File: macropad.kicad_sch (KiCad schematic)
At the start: 1 part, among them U1 RP2040

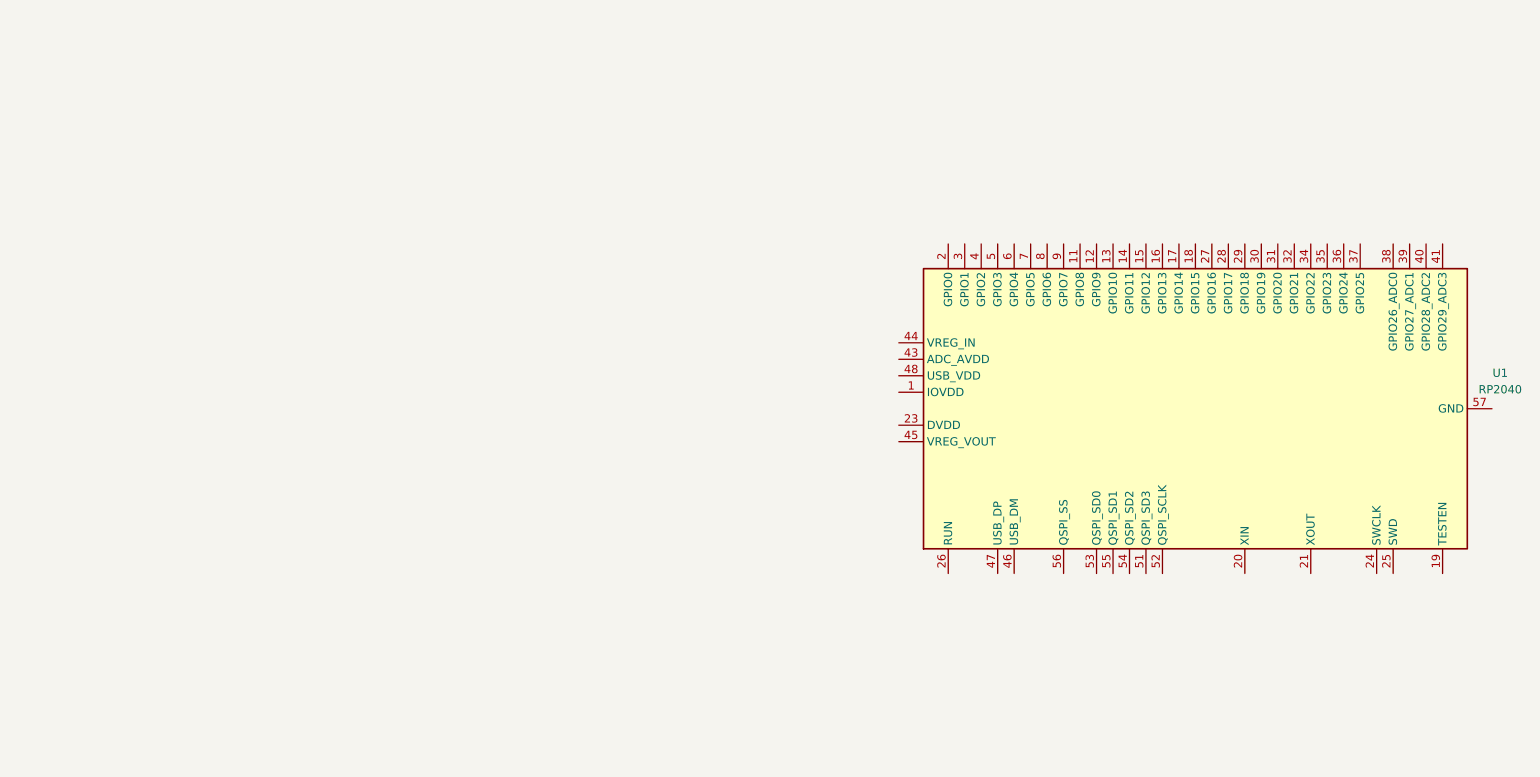
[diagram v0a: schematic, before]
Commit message: Make switches and rotary encoder
Got a rotary encoder switch and hooked it up to the MCU
Imported Joe Scotto's symbols and footprints for switches
Assigned footprint for diodes
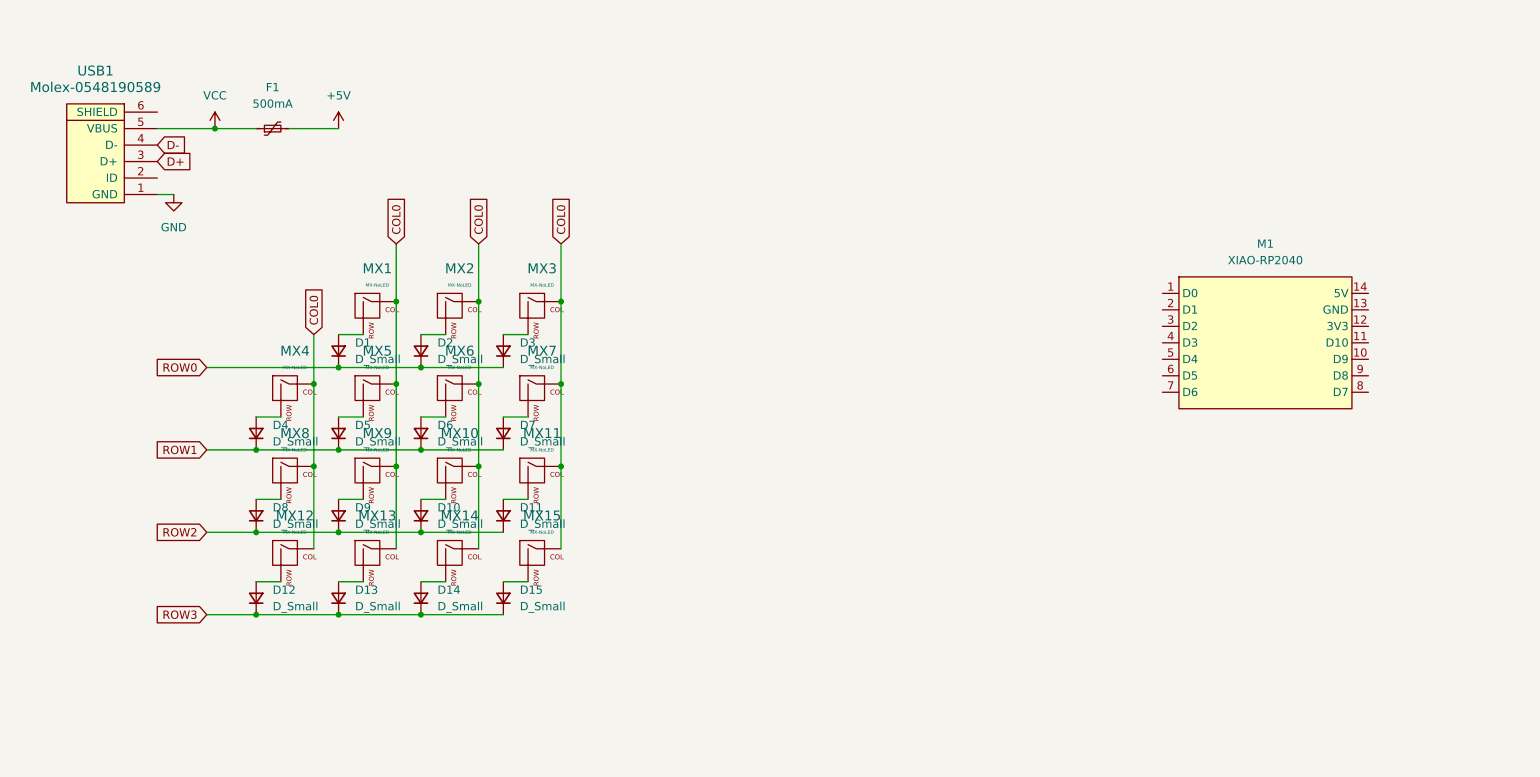
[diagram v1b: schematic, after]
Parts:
- removed U1: RP2040, Package_DFN_QFN:QFN-56-1EP_7x7mm_P0.4mm_EP3.2x3.2mm, symbol MCU_RaspberryPi:RP2040
- added D1, D10, D11, D12, D13, D14, D15, D2, D3, D4, D5, D6, D7, D8, D9: D_Small, symbol Device:D_Small
- added F1: 500mA, symbol Device:Polyfuse_Small
- added M1: XIAO-RP2040, symbol xiao-rp2040:XIAO-RP2040
- added MX1, MX10, MX11, MX12, MX13, MX14, MX15, MX2, MX3, MX4, MX5, MX6, MX7, MX8, MX9: MX-NoLED, symbol MX_Alps_Hybrid:MX-NoLED
- added USB1: Molex-0548190589, symbol random-keyboard-parts:Molex-0548190589
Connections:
- new net: D12.2 (A), MX12.2 (ROW)
- new net: D6.2 (A), MX6.2 (ROW)
- new net: D9.2 (A), MX9.2 (ROW)
- new net: D2.2 (A), MX2.2 (ROW)
- new net: D10.2 (A), MX10.2 (ROW)
- new net: D15.2 (A), MX15.2 (ROW)
- new net: D11.2 (A), MX11.2 (ROW)
- new net: D4.2 (A), MX4.2 (ROW)
- new net: D13.2 (A), MX13.2 (ROW)
- new net: D14.2 (A), MX14.2 (ROW)
- new net: D3.2 (A), MX3.2 (ROW)
- new net: D5.2 (A), MX5.2 (ROW)
- new net: D7.2 (A), MX7.2 (ROW)
- new net: D1.2 (A), MX1.2 (ROW)
- new net: D8.2 (A), MX8.2 (ROW)
- new net +5V: F1.2
- new net COL0: MX1.1 (COL), MX10.1 (COL), MX11.1 (COL), MX12.1 (COL), MX13.1 (COL), MX14.1 (COL), MX15.1 (COL), MX2.1 (COL), MX3.1 (COL), MX4.1 (COL), MX5.1 (COL), MX6.1 (COL), MX7.1 (COL), MX8.1 (COL), MX9.1 (COL)
- new net D+: USB1.3 (D+)
- new net D-: USB1.4 (D-)
- new net GND: USB1.1 (GND)
- new net ROW0: D1.1 (K), D2.1 (K), D3.1 (K)
- new net ROW1: D4.1 (K), D5.1 (K), D6.1 (K), D7.1 (K)
- new net ROW2: D10.1 (K), D11.1 (K), D8.1 (K), D9.1 (K)
- new net ROW3: D12.1 (K), D13.1 (K), D14.1 (K), D15.1 (K)
- new net VCC: F1.1, USB1.5 (VBUS)

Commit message: Create PCB file
Arranged components
Routed components
Outlined the PCB
Made filled zones
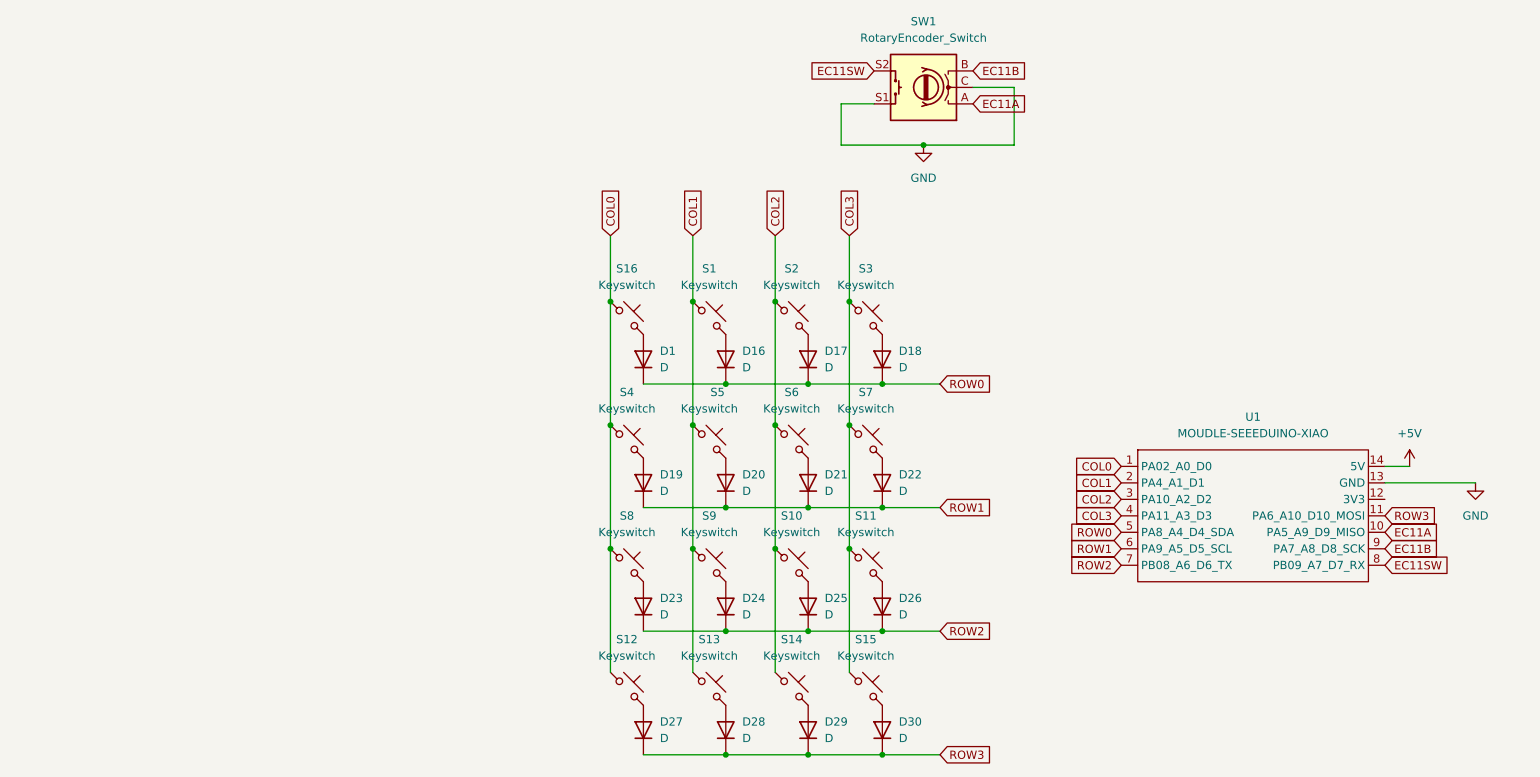
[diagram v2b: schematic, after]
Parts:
- removed D1, D10, D11, D12, D13, D14, D15, D2, D3, D4, D5, D6, D7, D8, D9: D_Small, symbol Device:D_Small
- removed F1: 500mA, symbol Device:Polyfuse_Small
- removed M1: XIAO-RP2040, symbol xiao-rp2040:XIAO-RP2040
- removed MX1, MX10, MX11, MX12, MX13, MX14, MX15, MX2, MX3, MX4, MX5, MX6, MX7, MX8, MX9: MX-NoLED, symbol MX_Alps_Hybrid:MX-NoLED
- removed USB1: Molex-0548190589, symbol random-keyboard-parts:Molex-0548190589
- added D1, D16, D17, D18, D19, D20, D21, D22, D23, D24, D25, D26, D27, D28, D29, D30: D, ScottoKeebs_Components:Diode_DO-35, symbol Device:D
- added S1, S10, S11, S12, S13, S14, S15, S16, S2, S3, S4, S5, S6, S7, S8, S9: Keyswitch, MX_Solderable:MX-Solderable-1U, symbol ScottoKeebs:Placeholder_Keyswitch
- added SW1: RotaryEncoder_Switch, Rotary_Encoder:RotaryEncoder_Alps_EC11E-Switch_Vertical_H20mm, symbol Device:RotaryEncoder_Switch
- added U1: MOUDLE-SEEEDUINO-XIAO, XIAO_PCB:MOUDLE14P-2.54-21X17.8MM, symbol MOUDLE-SEEEDUINO-XIAO:MOUDLE-SEEEDUINO-XIAO
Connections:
- net +5V: now also U1.14 (5V)
- net COL0: now also S12.1, S16.1, S4.1, S8.1, U1.1 (PA02_A0_D0)
- net GND: now also SW1.C, SW1.S1, U1.13 (GND)
- net ROW0: now also D1.1 (K), D16.1 (K), D17.1 (K), D18.1 (K), U1.5 (PA8_A4_D4_SDA)
- net ROW1: now also D19.1 (K), D20.1 (K), D21.1 (K), D22.1 (K), U1.6 (PA9_A5_D5_SCL)
- net ROW2: now also D23.1 (K), D24.1 (K), D25.1 (K), D26.1 (K), U1.7 (PB08_A6_D6_TX)
- net ROW3: now also D27.1 (K), D28.1 (K), D29.1 (K), D30.1 (K), U1.11 (PA6_A10_D10_MOSI)
- new net: D24.2 (A), S9.2
- new net: D29.2 (A), S14.2
- new net: D19.2 (A), S4.2
- new net: D20.2 (A), S5.2
- new net: D23.2 (A), S8.2
- new net: D16.2 (A), S1.2
- new net: D26.2 (A), S11.2
- new net: D28.2 (A), S13.2
- new net: D21.2 (A), S6.2
- new net: D22.2 (A), S7.2
- new net: D1.2 (A), S16.2
- new net: D25.2 (A), S10.2
- new net: D18.2 (A), S3.2
- new net: D30.2 (A), S15.2
- new net: D27.2 (A), S12.2
- new net: D17.2 (A), S2.2
- new net COL1: S1.1, S13.1, S5.1, S9.1, U1.2 (PA4_A1_D1)
- new net COL2: S10.1, S14.1, S2.1, S6.1, U1.3 (PA10_A2_D2)
- new net COL3: S11.1, S15.1, S3.1, S7.1, U1.4 (PA11_A3_D3)
- new net EC11A: SW1.A, U1.10 (PA5_A9_D9_MISO)
- new net EC11B: SW1.B, U1.9 (PA7_A8_D8_SCK)
- new net EC11SW: SW1.S2, U1.8 (PB09_A7_D7_RX)
